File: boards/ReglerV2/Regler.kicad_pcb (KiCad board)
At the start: 2 copper layers, 160 x 50 mm, 13 parts, among them J1 L_In, J2 R_In, J3 12V_In, J4 Switch, J5 L_Out, J6 R_Out, K1 DIPxx-2Axx-21x, K2 DIPxx-2Axx-21x, K3 DIPxx-2Axx-21x, K4 DIPxx-2Axx-21x

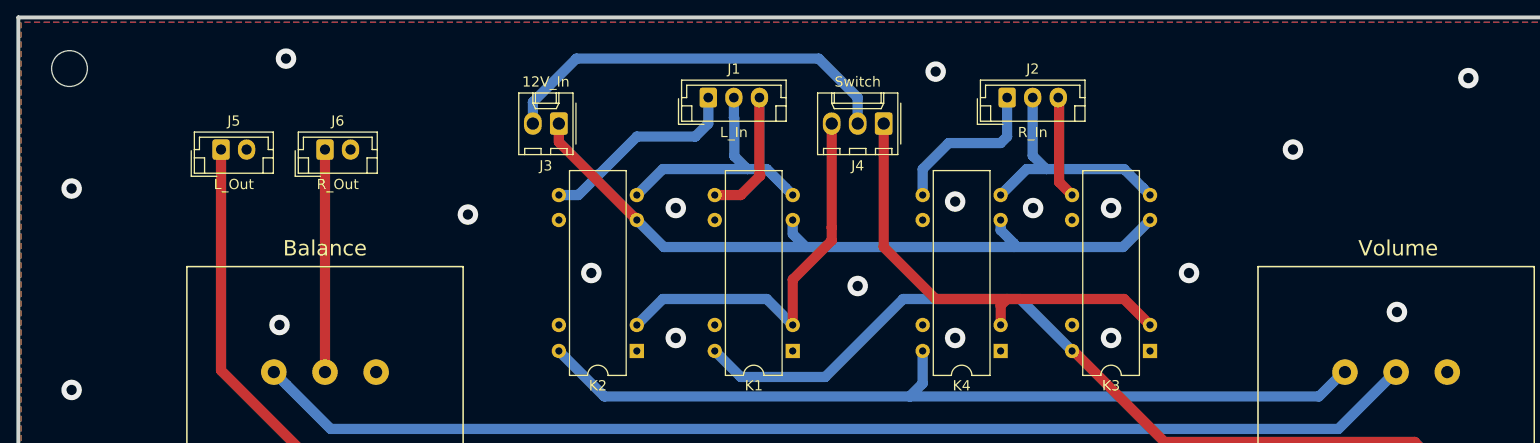
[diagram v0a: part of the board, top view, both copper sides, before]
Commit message: Added Power LEDs
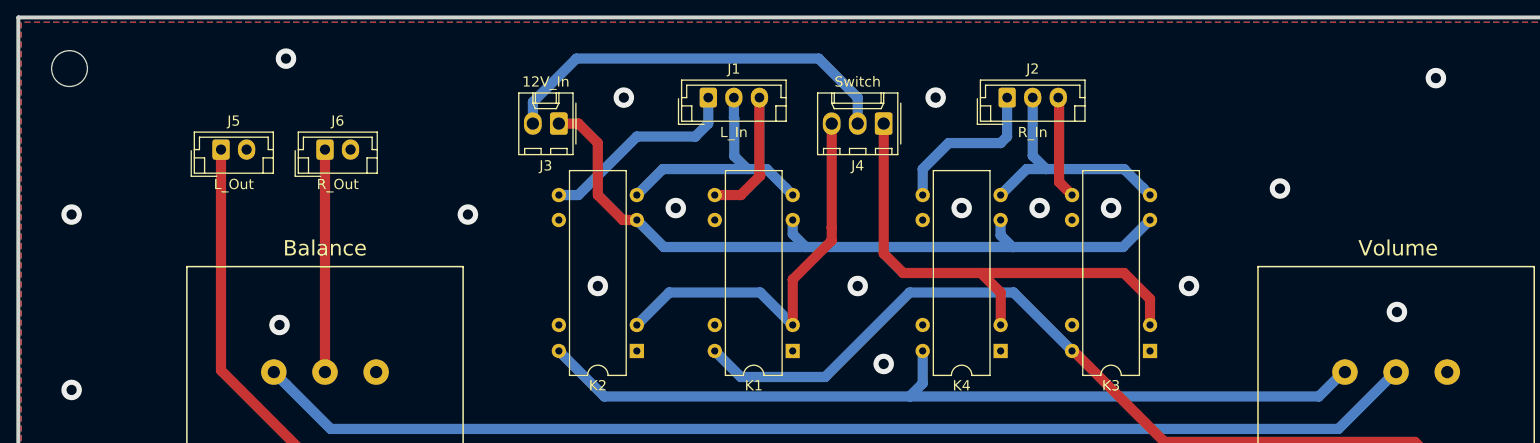
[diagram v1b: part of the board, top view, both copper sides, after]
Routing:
- net Net-(J4-Pad1): track 44.1 -> 49.0 mm
- net Net-(J3-Pad1): track 71.4 -> 73.4 mm
- net Net-(K1-Pad14): track 82.9 -> 83.4 mm
- net Net-(J4-Pad3): track 38.6 -> 39.1 mm
- net Earth_Clean: vias 23 -> 22

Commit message: Adjusted Silkscreen
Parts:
- J1: value L_In -> In_1
- J2: value R_In -> In_2
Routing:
- net Net-(K1-Pad14): track 83.4 -> 89.8 mm
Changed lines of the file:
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@@
     (thickness 1.6)
     (drawings 2)
-    (tracks 124)
+    (tracks 123)
     (zones 0)
     (modules 13)
@@
       (effects (font (size 1 1) (thickness 0.15)))
     )
-    (fp_text value R_In (at 2.5 3.4) (layer F.SilkS)
+    (fp_text value In_2 (at 2.5 3.4) (layer F.SilkS)
       (effects (font (size 1 1) (thickness 0.15)))
     )
@@
       (effects (font (size 1 1) (thickness 0.15)))
     )
-    (fp_text value L_In (at 2.5 3.4) (layer F.SilkS)
+    (fp_text value In_1 (at 2.5 3.4) (layer F.SilkS)
       (effects (font (size 1 1) (thickness 0.15)))
     )
@@
   (segment (start 142.24 102.235) (end 144.78 99.695) (width 1) (layer B.Cu) (net 9))
   (segment (start 192.265321 130.830321) (end 193.515 132.08) (width 1) (layer F.Cu) (net 10))
-  (segment (start 190.34 128.905) (end 192.265321 130.830321) (width 1) (layer F.Cu) (net 10))
-  (segment (start 165.875025 128.905) (end 190.34 128.905) (width 1) (layer F.Cu) (net 10))
-  (segment (start 156.845 120.015) (end 156.985025 120.015) (width 1) (layer F.Cu) (net 10))
-  (segment (start 156.985025 120.015) (end 165.875025 128.905) (width 1) (layer F.Cu) (net 10))
-  (segment (start 151.13 114.3) (end 156.845 120.015) (width 1) (layer B.Cu) (net 10))
-  (segment (start 140.97 114.3) (end 151.13 114.3) (width 1) (layer B.Cu) (net 10))
-  (segment (start 132.715 122.555) (end 140.97 114.3) (width 1) (layer B.Cu) (net 10))
-  (segment (start 121.92 120.015) (end 124.46 122.555) (width 1) (layer B.Cu) (net 10))
-  (segment (start 124.46 122.555) (end 132.715 122.555) (width 1) (layer B.Cu) (net 10))
+  (segment (start 187.8 126.365) (end 192.265321 130.830321) (width 1) (layer F.Cu) (net 10))
+  (segment (start 163.335025 126.365) (end 187.8 126.365) (width 1) (layer F.Cu) (net 10))
+  (segment (start 159.385 126.365) (end 163.335025 126.365) (width 1) (layer F.Cu) (net 10))
+  (segment (start 156.845 120.015) (end 156.845 123.825) (width 1) (layer F.Cu) (net 10))
+  (segment (start 156.845 123.825) (end 159.385 126.365) (width 1) (layer F.Cu) (net 10))
+  (segment (start 121.92 123.19) (end 121.92 120.015) (width 1) (layer F.Cu) (net 10))
+  (segment (start 163.335025 126.365) (end 125.095 126.365) (width 1) (layer F.Cu) (net 10))
+  (segment (start 125.095 126.365) (end 121.92 123.19) (width 1) (layer F.Cu) (net 10))
   (segment (start 183.355 122.08) (end 183.515 122.08) (width 1) (layer B.Cu) (net 11))
   (segment (start 180.975 124.46) (end 183.355 122.08) (width 1) (layer B.Cu) (net 11))

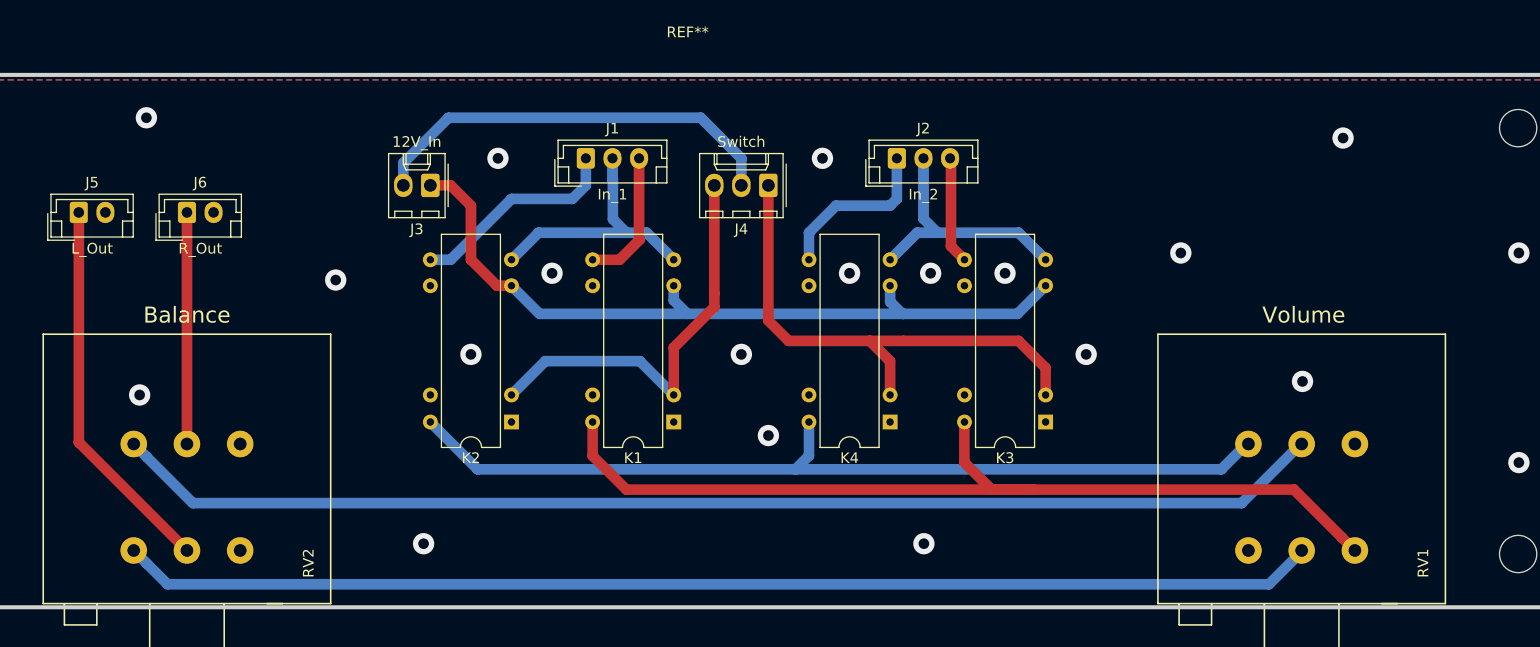
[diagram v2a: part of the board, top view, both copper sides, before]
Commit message: Added Mounting holes, Moved -60V Divider to HV Board, eliminated +450V Connector and Feedback Connector on Amp Board
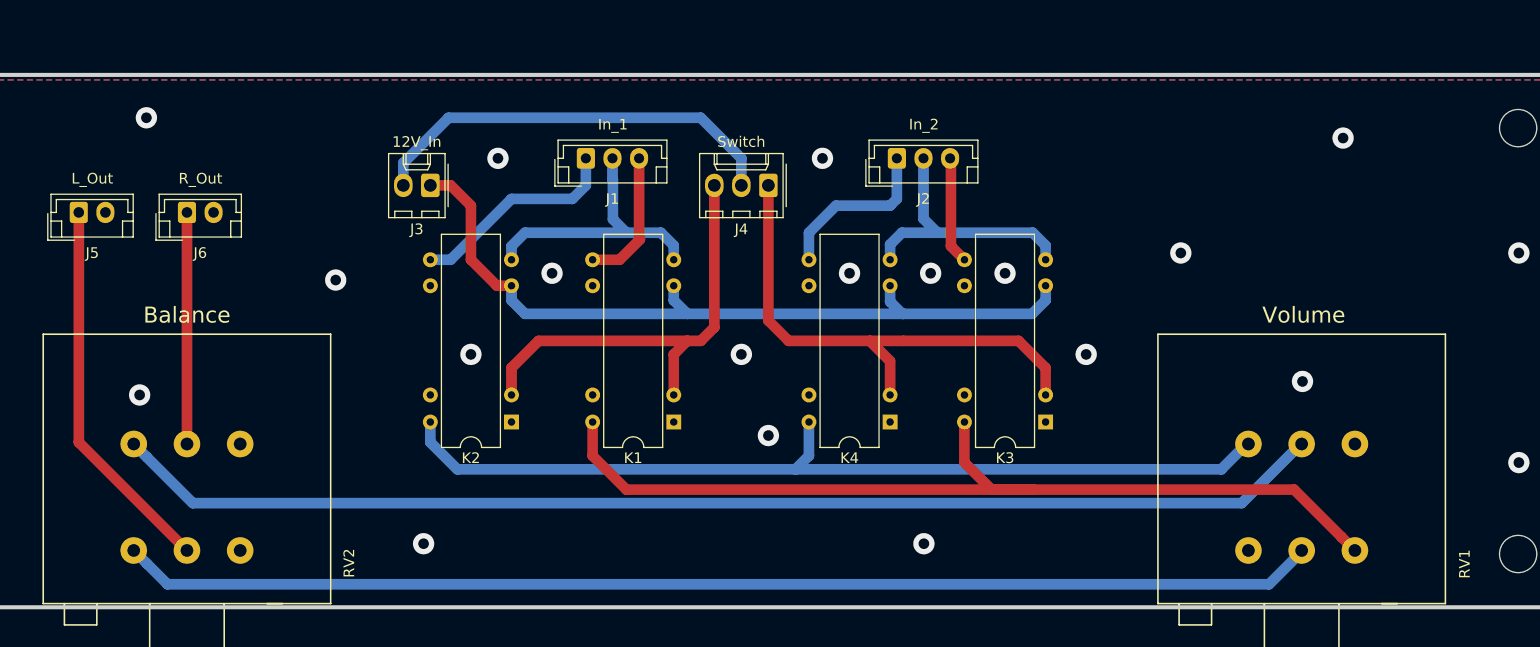
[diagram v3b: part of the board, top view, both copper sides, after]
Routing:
- net Net-(J4-Pad3): track 39.1 -> 42.1 mm
- net Net-(J2-Pad2): track 24.2 -> 25.9 mm
- net Net-(J3-Pad1): track 73.4 -> 75.0 mm
- net Net-(J1-Pad2): track 24.9 -> 26.4 mm
- net Net-(K2-Pad14): track 84.6 -> 85.7 mm

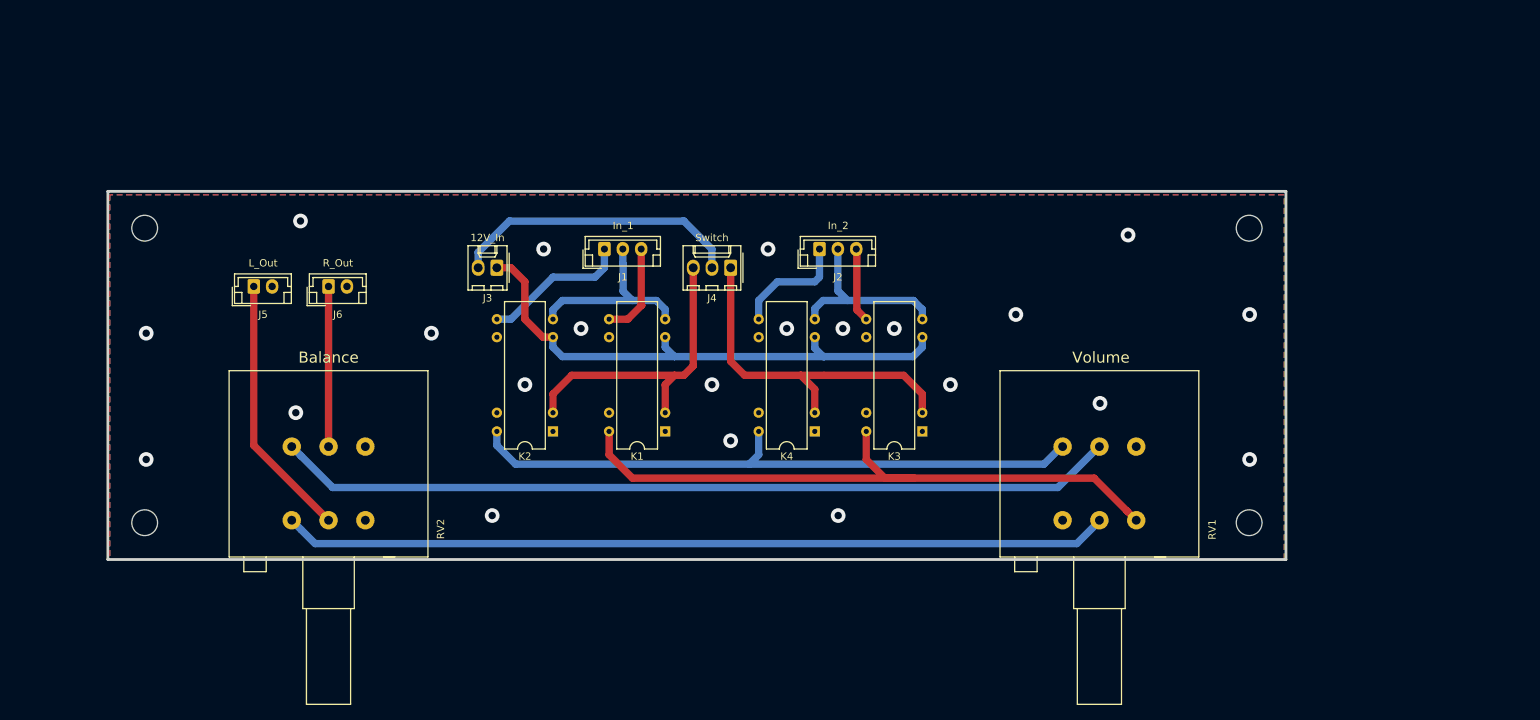
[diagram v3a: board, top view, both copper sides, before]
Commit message: 6,3V und 12V auf einer Platine zusammengefasst
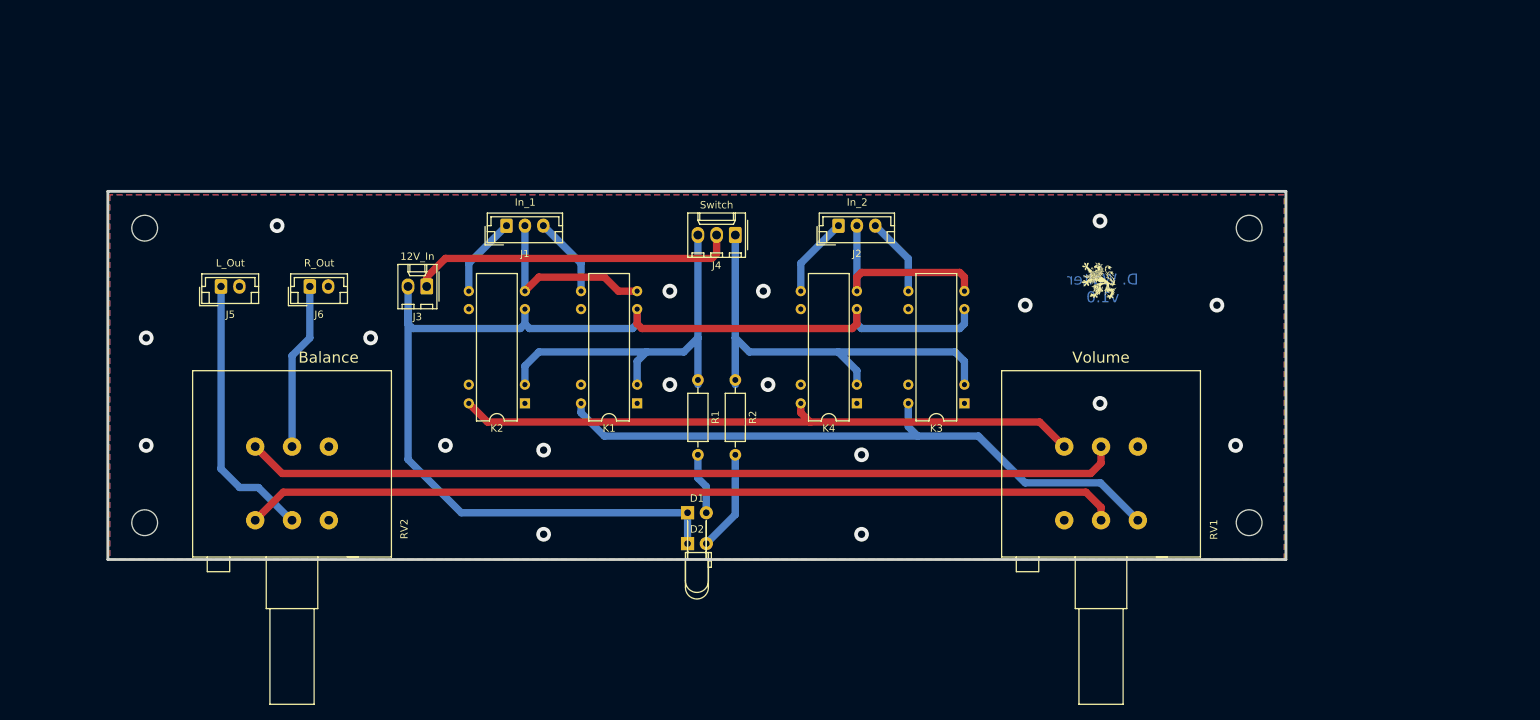
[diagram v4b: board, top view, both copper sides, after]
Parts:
- added D1: LED_1, LED_THT:LED_D3.0mm_Horizontal_O6.35mm_Z6.0mm, F.Cu at (132.6, 131.1)
- added D2: LED_2, LED_THT:LED_D3.0mm_Horizontal_O1.27mm_Z2.0mm, F.Cu at (132.6, 135.3)
- added G***: LOGO, Loewe:Loewe_Klein, F.Cu at (188.5, 99.6)
- added R1: R, Resistor_THT:R_Axial_DIN0207_L6.3mm_D2.5mm_P10.16mm_Horizontal, F.Cu at (134.0, 113.0)
- added R2: R, Resistor_THT:R_Axial_DIN0207_L6.3mm_D2.5mm_P10.16mm_Horizontal, F.Cu at (139.1, 113.0)
- moved J1 13.7 mm to (108.0, 92.1)
- moved J3 9.86 mm to (97.2, 100.3)
- moved K3 6.87 mm to (170.2, 116.2)
- moved K4 6.87 mm to (155.6, 116.2)
- moved K2 5.39 mm to (110.5, 116.2)
- moved K1 5.39 mm to (125.7, 116.2)
- moved RV2 4.96 mm to (83.9, 133.3)
- moved J4 4.49 mm to (139.1, 93.3)
- moved J5 4.44 mm to (69.2, 100.3)
- moved J2 4.09 mm to (153.1, 92.1)
- moved J6 2.54 mm to (81.3, 100.3)
- moved RV1 0.22 mm to (193.7, 133.3)
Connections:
- net Net-(J1-Pad1) renamed /R_1
- net Net-(J1-Pad2) renamed /GND_1
- net Net-(J1-Pad3) renamed /L_1
- net Net-(J2-Pad1) renamed /R_2
- net Net-(J2-Pad2) renamed /GND_2
- net Net-(J2-Pad3) renamed /L_2
- net Net-(J4-Pad1) renamed /CH_2
- net Net-(J4-Pad3) renamed /CH_1
- net Net-(J5-Pad1) renamed /L_Out
- net Net-(J6-Pad1) renamed /R_Out
- net Net-(K1-Pad14) renamed /L_Sw
- net Net-(K2-Pad14) renamed /R_Sw
- J3 pad 1: Net-(J3-Pad1) -> +12V
- J3 pad 2: Net-(J3-Pad2) -> GND
- J4 pad 2: Net-(J3-Pad2) -> +12V
- K1 pad 6: Net-(J3-Pad1) -> GND
- K2 pad 6: Net-(J3-Pad1) -> GND
- K3 pad 6: Net-(J3-Pad1) -> GND
- K4 pad 6: Net-(J3-Pad1) -> GND
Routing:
- net GND: track 0.00 -> 160.3 mm
- net Net-(J3-Pad1): track 75.0 -> 0.00 mm
- net +12V: track 0.00 -> 44.5 mm
- net Net-(J3-Pad2): track 39.7 -> 0.00 mm
- net Net-(D2-Pad2): track 0.00 -> 13.1 mm
- net /CH_2: track 49.0 -> 61.4 mm
- net /CH_1: track 42.1 -> 52.9 mm
- net /R_1: track 20.0 -> 11.0 mm
- net Net-(D1-Pad2): track 0.00 -> 7.71 mm
- net Net-(RV1-Pad2): track 112.4 -> 119.1 mm
- net Net-(RV1-Pad5): track 114.3 -> 119.2 mm
- net /R_2: track 15.9 -> 11.0 mm
- net /GND_2: track 25.9 -> 27.8 mm
- net /L_Sw: track 89.8 -> 87.9 mm
- net /L_1: track 12.9 -> 11.0 mm
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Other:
- board text added: "D. Walter v1.0"

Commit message: Reworked Delay + Layout changed
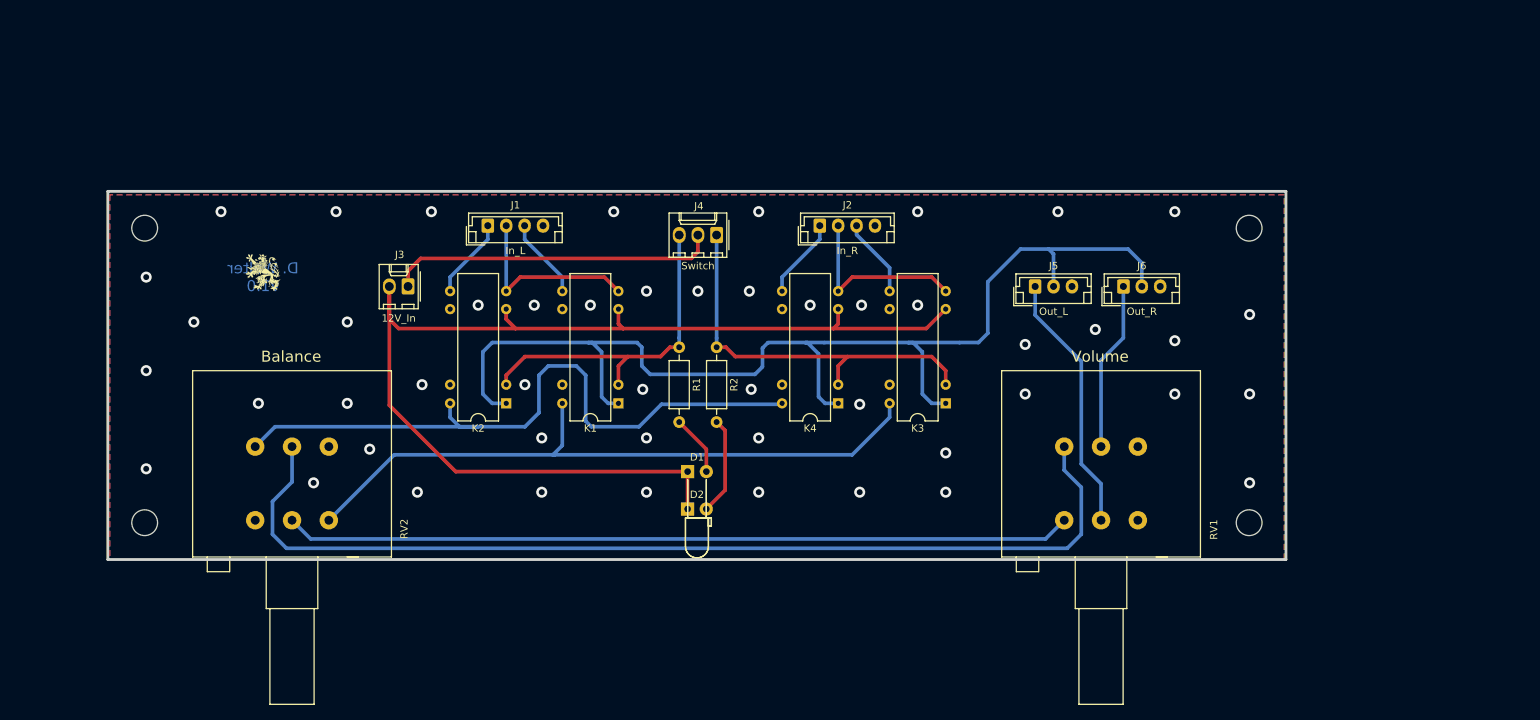
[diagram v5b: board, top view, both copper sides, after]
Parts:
- D1: value LED_1 -> LED_1 Gn
- D2: value LED_2 -> LED_2 Gn; footprint LED_THT:LED_D3.0mm_Horizontal_O1.27mm_Z2.0mm -> LED_THT:LED_D3.0mm_Horizontal_O1.27mm_Z6.0mm
- J1: value In_1 -> In_L; footprint Connector_JST:JST_EH_B3B-EH-A_1x03_P2.50mm_Vertical -> Connector_JST:JST_EH_B4B-EH-A_1x04_P2.50mm_Vertical
- J2: value In_2 -> In_R; footprint Connector_JST:JST_EH_B3B-EH-A_1x03_P2.50mm_Vertical -> Connector_JST:JST_EH_B4B-EH-A_1x04_P2.50mm_Vertical
- J5: value L_Out -> Out_L; footprint Connector_JST:JST_EH_B2B-EH-A_1x02_P2.50mm_Vertical -> Connector_JST:JST_EH_B3B-EH-A_1x03_P2.50mm_Vertical
- J6: value R_Out -> Out_R; footprint Connector_JST:JST_EH_B2B-EH-A_1x02_P2.50mm_Vertical -> Connector_JST:JST_EH_B3B-EH-A_1x03_P2.50mm_Vertical
- R1, R2: value R -> 560R
- RV1: value Alps 50k lin -> Alps 20k log
- RV2: value Alps 20k log -> Alps 50k lin
- moved G*** 113.5 mm to (74.9, 98.4)
- moved J5 110.6 mm to (179.8, 100.3)
- moved J6 110.5 mm to (191.8, 100.3)
- moved D1 5.59 mm to (132.6, 125.5)
- moved R1 5.12 mm to (131.4, 108.6)
- moved R2 5.12 mm to (136.5, 108.6)
- moved D2 4.70 mm to (132.6, 130.6)
- moved K3 2.54 mm to (167.6, 116.2)
- moved J3 2.54 mm to (94.6, 100.3)
- moved K1 2.54 mm to (123.2, 116.2)
- moved J1 2.54 mm to (105.5, 92.1)
- moved J2 2.54 mm to (150.5, 92.1)
- moved J4 2.54 mm to (136.5, 93.3)
- moved K2 2.54 mm to (108.0, 116.2)
- moved K4 2.54 mm to (153.0, 116.2)
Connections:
- J5 pad 2: Earth_Clean -> GNDS
- J6 pad 2: Earth_Clean -> GNDS
- K1 pad 1: Earth_Clean -> GNDS
- K2 pad 1: Earth_Clean -> GNDS
- K3 pad 1: Earth_Clean -> GNDS
- K4 pad 1: Earth_Clean -> GNDS
- RV1 pad 1: Earth_Clean -> Net-(RV1-Pad1)
- RV1 pad 2: Net-(RV1-Pad2) -> /L_Out
- RV1 pad 3: /L_Sw -> Earth_Clean
- RV1 pad 4: /R_Sw -> Net-(RV1-Pad4)
- RV1 pad 5: Net-(RV1-Pad5) -> /R_Out
- RV2 pad 1: Net-(RV1-Pad2) -> (no net)
- RV2 pad 2: /L_Out -> Net-(RV1-Pad1)
- RV2 pad 3: Earth_Clean -> /L_Sw
- RV2 pad 4: Net-(RV1-Pad5) -> /R_Sw
- RV2 pad 5: /R_Out -> Net-(RV1-Pad4)
- RV2 pad 6: Earth_Clean -> (no net)
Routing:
- net GNDS: track 0.00 -> 158.9 mm
- net Net-(RV1-Pad4): track 0.00 -> 137.3 mm
- net Net-(RV1-Pad5): track 119.2 -> 0.00 mm
- net Net-(RV1-Pad2): track 119.1 -> 0.00 mm
- net Net-(RV1-Pad1): track 0.00 -> 107.1 mm
- net /CH_2: track 61.4 -> 53.9 mm
- net /R_Sw: track 86.4 -> 93.7 mm
- net /CH_1: track 52.9 -> 45.9 mm
- net GND: track 160.3 -> 156.1 mm
- net /L_Sw: track 87.9 -> 91.6 mm
- net /GND_2: track 27.8 -> 25.1 mm
- net /L_Out: track 37.3 -> 35.5 mm
- net Net-(D1-Pad2): track 7.71 -> 8.26 mm
- net Earth_Clean: vias 18 -> 49
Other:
- net class Default: via_dia 2 -> 1.5; via_drill 1 -> 0.8
